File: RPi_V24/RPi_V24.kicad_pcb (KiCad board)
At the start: 4 copper layers, 65 x 56 mm, 61 parts, among them J1 DB9_Male, J10 Conn_01x03, J11 Conn_01x03, J12 Conn_01x03_Female, J13 Conn_02x04_Odd_Even, J14 Conn_01x03, J15 Conn_01x03, J16 Conn_02x05_Odd_Even, J17 Conn_02x05_Odd_Even, J18 Conn_02x05_Odd_Even, J2 DB9_Male, J3 40HAT, J4 DB9_Male, J5 Conn_02x04_Odd_Even, J6 Conn_01x03, J7 Conn_01x03, J8 Conn_02x04_Odd_Even, J9 CONN_01X02, U1 MAX561, U2 CAT24C32, U3 MAX561

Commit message: Now includes EN and SHDN for the transceivers.
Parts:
- added R16: 10K, Resistor_SMD:R_0402_1005Metric, F.Cu at (108.1, 91.6)
- added R17: 0R, Resistor_SMD:R_0402_1005Metric, F.Cu at (108.1, 89.7)
- added R18: 10K, Resistor_SMD:R_0402_1005Metric, F.Cu at (102.1, 72.3)
- added R19: 0R, Resistor_SMD:R_0402_1005Metric, F.Cu at (98.3, 73.9)
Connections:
- J13 pad 1: Net-(J13-Pad1) -> TXD4E
- J13 pad 7: Net-(J13-Pad7) -> RXD4E
- J3 pad 13: Net-(J3-Pad13) -> ~EN4_5
- J3 pad 15: Net-(J3-Pad15) -> SHDN4_5
- J3 pad 3: Net-(J3-Pad3) -> SHDN1_3
- J3 pad 5: Net-(J3-Pad5) -> ~EN1_3
- J5 pad 1: Net-(J5-Pad1) -> TXD1E
- J5 pad 7: Net-(J5-Pad7) -> RXD1E
- J8 pad 1: Net-(J8-Pad1) -> TXD3E
- J8 pad 7: Net-(J8-Pad7) -> RXD3E
- U1 pad 24: Net-(U1-Pad24) -> ~EN1_3
- U1 pad 25: Net-(U1-Pad25) -> SHDN1_3
- U3 pad 24: Net-(U3-Pad24) -> ~EN4_5
- U3 pad 25: Net-(U3-Pad25) -> SHDN4_5
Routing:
- net SHDN1_3: track 0.00 -> 50.4 mm, vias 0 -> 3
- net ~EN1_3: track 0.00 -> 46.5 mm, vias 0 -> 3
- net ~EN4_5: track 0.00 -> 16.6 mm, vias 0 -> 1
- net SHDN4_5: track 0.00 -> 10.1 mm, vias 0 -> 1
- net RXD3E: track 13.0 -> 15.8 mm
- net TX4DE: track 2.54 -> 0.00 mm
- net TX1DE: track 2.54 -> 0.00 mm
- net RXD4E: track 13.2 -> 15.7 mm
- net RX4DE: track 2.54 -> 0.00 mm
- net RX3DE: track 2.54 -> 0.00 mm
- net TXD1E: track 9.31 -> 11.9 mm
- net TXD3E: track 20.1 -> 22.7 mm
- net TX3DE: track 2.54 -> 0.00 mm
- net RXD1E: track 17.8 -> 20.3 mm
- net RX1DE: track 2.54 -> 0.00 mm
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
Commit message: Adds layer identifiers
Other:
- board text added: "1"
- board text added: "2"
- board text added: "3"
- board text added: "4"
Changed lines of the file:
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@@
   (general
     (thickness 1.6)
-    (drawings 131)
+    (drawings 135)
     (tracks 735)
     (zones 0)
@@
   (layers
     (0 F.Cu signal)
-    (1 In1.Cu power hide)
-    (2 In2.Cu power hide)
+    (1 In1.Cu power)
+    (2 In2.Cu power)
     (31 B.Cu signal)
     (32 B.Adhes user)
@@
       (drillshape 0)
       (scaleselection 1)
-      (outputdirectory "prod"))
+      (outputdirectory "../gerber/"))
   )
   (net 0 "")
@@
     )
   )
+  (gr_text 4 (at 126.238 115.316) (layer B.Cu)
+    (effects (font (size 1.5 1.5) (thickness 0.3)) (justify mirror))
+  )
+  (gr_text 3 (at 124.587 115.316) (layer In2.Cu)
+    (effects (font (size 1.5 1.5) (thickness 0.3)))
+  )
+  (gr_text 2 (at 122.809 115.316) (layer In1.Cu)
+    (effects (font (size 1.5 1.5) (thickness 0.3)))
+  )
+  (gr_text 1 (at 121.031 115.316) (layer F.Cu)
+    (effects (font (size 1.5 1.5) (thickness 0.3)))
+  )
   (gr_text + (at 89.408 106.68) (layer F.SilkS)
     (effects (font (size 0.6 0.6) (thickness 0.09)))
@@
       )
     )
+  )
+  (zone (net 0) (net_name "") (layers In1.Cu In2.Cu) (hatch edge 0.508)
+    (connect_pads (clearance 0.4))
+    (min_thickness 0.254)
+    (keepout (tracks allowed) (vias allowed) (copperpour not_allowed))
+    (fill (arc_segments 32) (thermal_gap 0.508) (thermal_bridge_width 0.508))
+    (polygon
+      (pts
+        (xy 127.254 117.221) (xy 120.015 117.221) (xy 120.015 113.665) (xy 127.254 113.665)
+      )
+    )

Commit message: Some final touches and some generated files.
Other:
- rule pad_to_mask_clearance: 0.1 -> 0.15
- board text added: "JLCJLCJLCJLC"
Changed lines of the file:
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@@
   (general
     (thickness 1.6)
-    (drawings 135)
+    (drawings 136)
     (tracks 735)
     (zones 0)
@@
     (pad_size 1.524 1.524)
     (pad_drill 0.762)
-    (pad_to_mask_clearance 0.1)
+    (pad_to_mask_clearance 0.15)
+    (solder_mask_min_width 0.153)
     (aux_axis_origin 0 0)
     (visible_elements 7FFFFE3F)
     (pcbplotparams
-      (layerselection 0x010f8_80000007)
+      (layerselection 0x010f8_ffffffff)
       (usegerberextensions false)
       (usegerberattributes false)
@@
     )
   )
+  (gr_text JLCJLCJLCJLC (at 104.521 76.708) (layer F.SilkS)
+    (effects (font (size 0.8 0.8) (thickness 0.15)))
+  )
   (gr_text 4 (at 126.238 115.316) (layer B.Cu)
     (effects (font (size 1.5 1.5) (thickness 0.3)) (justify mirror))
@@
   (segment (start 87.63 86.9525) (end 86.986999 87.595501) (width 0.25) (layer F.Cu) (net 66))
   (segment (start 93.853 79.121) (end 93.853 80.221) (width 0.25) (layer F.Cu) (net 66))
-  (segment (start 125.984 83.439) (end 125.984 85.979) (width 0.25) (layer F.Cu) (net 105))
-  (segment (start 125.984 89.721081) (end 125.984 91.059) (width 0.25) (layer F.Cu) (net 106))
-  (segment (start 125.984 88.519) (end 125.984 89.721081) (width 0.25) (layer F.Cu) (net 106))
-  (segment (start 107.442 99.314) (end 109.982 99.314) (width 0.25) (layer F.Cu) (net 108))
-  (segment (start 112.522 99.314) (end 115.062 99.314) (width 0.25) (layer F.Cu) (net 107))
-  (segment (start 96.393 89.594081) (end 96.393 90.932) (width 0.25) (layer F.Cu) (net 112))
-  (segment (start 96.393 88.392) (end 96.393 89.594081) (width 0.25) (layer F.Cu) (net 112))
-  (segment (start 96.393 83.312) (end 96.393 85.852) (width 0.25) (layer F.Cu) (net 111))
   (segment (start 134.8565 105.872) (end 135.001 105.7275) (width 0.15) (layer F.Cu) (net 75))
   (segment (start 133.35 105.872) (end 134.8565 105.872) (width 0.15) (layer F.Cu) (net 75))
@@
   (segment (start 89.027 86.36) (end 86.868 84.201) (width 0.25) (layer B.Cu) (net 104))
   (segment (start 89.027 87.0105) (end 89.027 86.36) (width 0.25) (layer B.Cu) (net 104))
+  (segment (start 125.984 83.439) (end 125.984 85.979) (width 0.25) (layer F.Cu) (net 105))
   (segment (start 126.1704 86.42901) (end 126.302205 86.297205) (width 0.25) (layer F.Cu) (net 105))
   (segment (start 122.428 83.693) (end 125.16401 86.42901) (width 0.25) (layer F.Cu) (net 105))
@@
   (segment (start 125.16401 86.42901) (end 126.1704 86.42901) (width 0.25) (layer F.Cu) (net 105))
   (segment (start 119.0675 84.914) (end 119.0675 84.26091) (width 0.25) (layer F.Cu) (net 105))
+  (segment (start 125.984 89.721081) (end 125.984 91.059) (width 0.25) (layer F.Cu) (net 106))
+  (segment (start 125.984 88.519) (end 125.984 89.721081) (width 0.25) (layer F.Cu) (net 106))
   (segment (start 123.317 82.705842) (end 123.317 82.423) (width 0.25) (layer B.Cu) (net 106))
   (segment (start 123.317 85.852) (end 123.317 82.705842) (width 0.25) (layer B.Cu) (net 106))
@@
   (segment (start 115.697 82.423) (end 123.034158 82.423) (width 0.25) (layer F.Cu) (net 106))
   (segment (start 123.034158 82.423) (end 123.317 82.423) (width 0.25) (layer F.Cu) (net 106))
+  (segment (start 112.522 99.314) (end 115.062 99.314) (width 0.25) (layer F.Cu) (net 107))
   (via (at 121.666 84.963) (size 0.4) (drill 0.2) (layers F.Cu B.Cu) (net 107))
   (segment (start 121.617 84.914) (end 121.666 84.963) (width 0.25) (layer F.Cu) (net 107))
@@
   (segment (start 112.522 99.314) (end 121.666 90.17) (width 0.25) (layer B.Cu) (net 107))
   (segment (start 121.666 85.245842) (end 121.666 84.963) (width 0.25) (layer B.Cu) (net 107))
+  (segment (start 107.442 99.314) (end 109.982 99.314) (width 0.25) (layer F.Cu) (net 108))
   (segment (start 119.0675 90.114) (end 119.0675 91.386504) (width 0.25) (layer F.Cu) (net 108))
   (segment (start 119.0675 91.386504) (end 118.616002 91.838002) (width 0.25) (layer F.Cu) (net 108))
@@
   (segment (start 101.0035 72.8095) (end 98.6155 70.4215) (width 0.25) (layer F.Cu) (net 110))
   (segment (start 101.0035 74.5315) (end 101.0035 72.8095) (width 0.25) (layer F.Cu) (net 110))
+  (segment (start 96.393 83.312) (end 96.393 85.852) (width 0.25) (layer F.Cu) (net 111))
   (via (at 98.933 85.598) (size 0.4) (drill 0.2) (layers F.Cu B.Cu) (net 111))
   (segment (start 98.679 85.852) (end 96.393 85.852) (width 0.25) (layer B.Cu) (net 111))
@@
   (segment (start 105.4485 80.5815) (end 104.369 81.661) (width 0.25) (layer F.Cu) (net 111))
   (segment (start 105.4485 79.7315) (end 105.4485 80.5815) (width 0.25) (layer F.Cu) (net 111))
+  (segment (start 96.393 89.594081) (end 96.393 90.932) (width 0.25) (layer F.Cu) (net 112))
+  (segment (start 96.393 88.392) (end 96.393 89.594081) (width 0.25) (layer F.Cu) (net 112))
   (segment (start 98.298 85.85059) (end 96.074795 88.073795) (width 0.25) (layer F.Cu) (net 112))
   (segment (start 98.298 83.187002) (end 98.298 85.85059) (width 0.25) (layer F.Cu) (net 112))

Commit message: Silk screen adjustments.
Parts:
- R17, R19: value 0R -> 10K

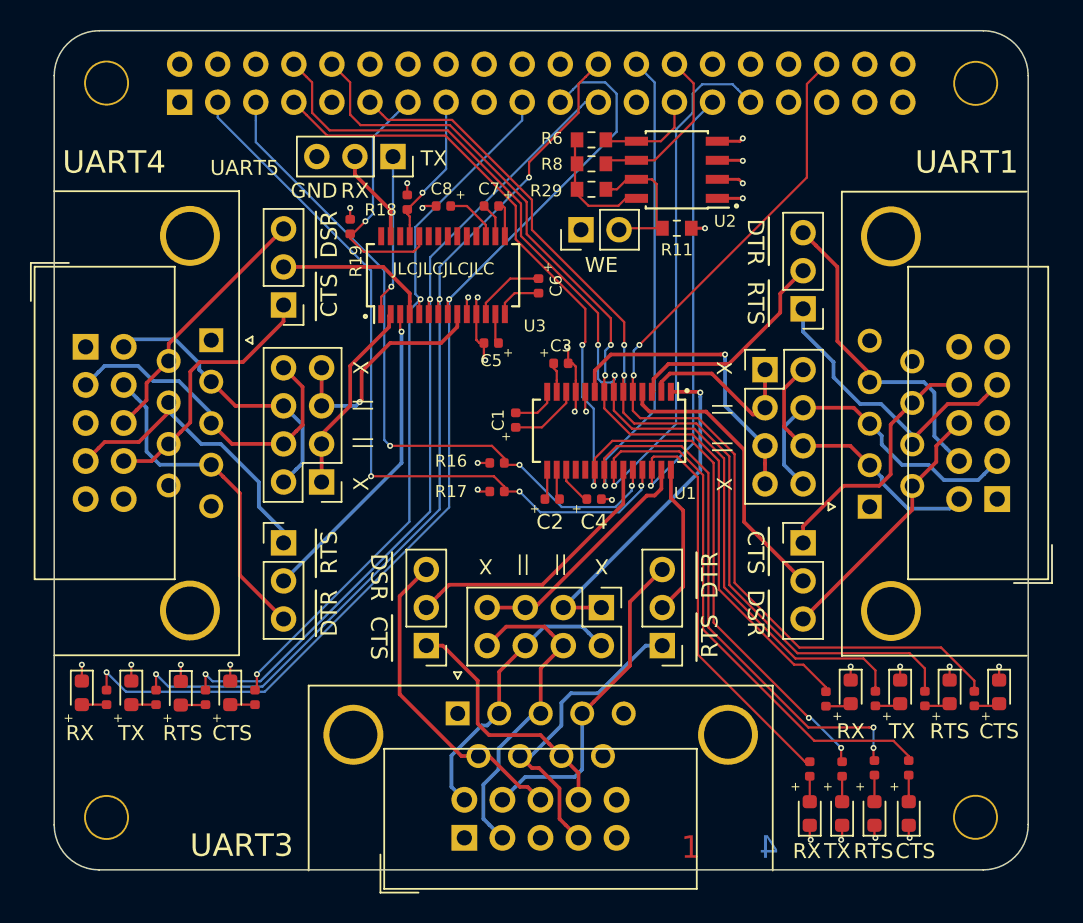
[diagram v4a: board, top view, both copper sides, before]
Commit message: Adjusts some component and trace positions
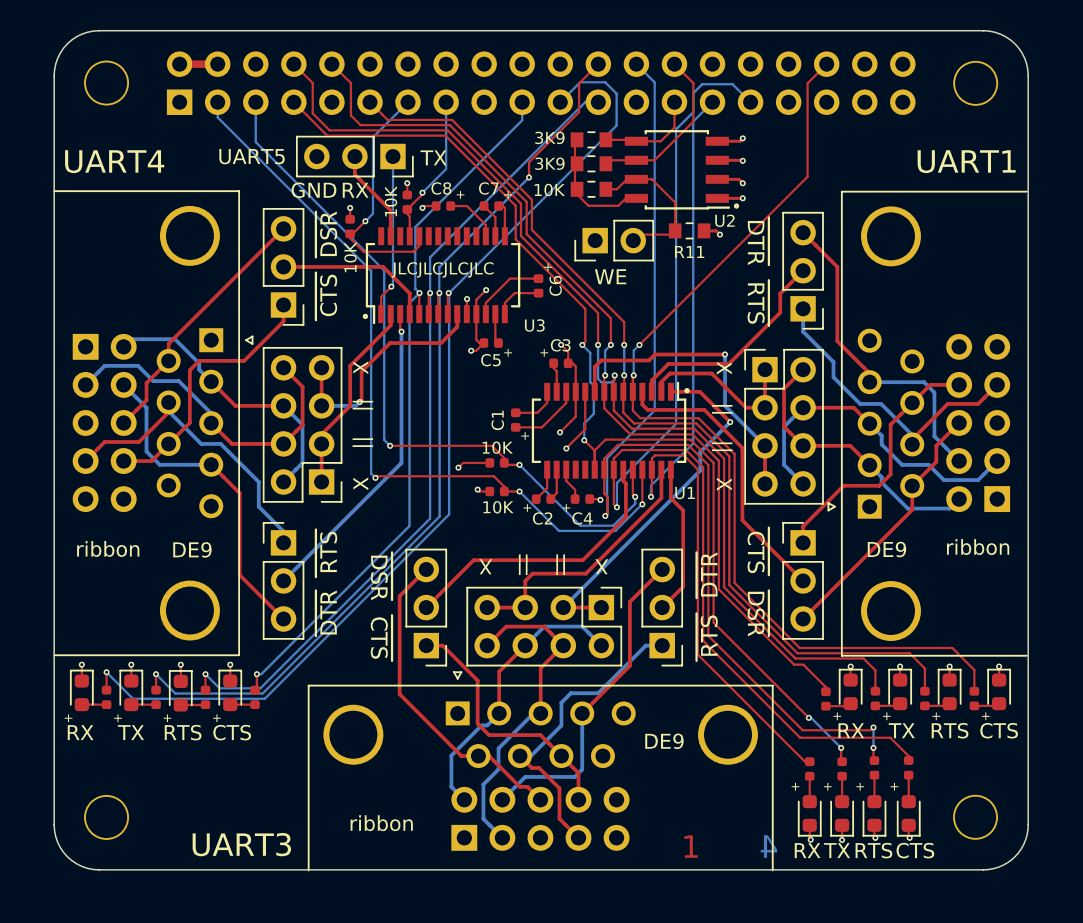
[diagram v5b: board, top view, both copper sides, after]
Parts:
- added G***: LOGO, LOGO, B.Cu at (111.5, 87.6)
- moved J9 1.20 mm to (114.7, 74.8)
- moved R11 0.87 mm to (121.0, 74.2)
- moved C4 0.78 mm to (113.8, 92.1)
- moved C2 0.58 mm to (111.2, 92.1)
- renumbered R29 to 10K, R16 to 10K, R17 to 10K, R18 to 10K, R19 to 10K, R8 to 3K9, R6 to 3K9
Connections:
- net ~EN1_3 renamed ~{EN1_3}
- net ~EN4_5 renamed ~{EN4_5}
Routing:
- net RTS3: track 66.2 -> 71.3 mm
- net GND: track 25.2 -> 29.8 mm
- net CTS3: track 69.4 -> 73.1 mm
- net P3V3_HAT: track 11.1 -> 13.8 mm
- net /P5V_HAT: track 0.00 -> 2.54 mm
- net RXD3: track 55.1 -> 57.0 mm
- net ~{EN1_3}: track 46.5 -> 48.3 mm
- net RXD3E: track 15.8 -> 17.6 mm
- net TXD3E: track 22.7 -> 24.3 mm
- net SHDN1_3: track 50.4 -> 52.0 mm
- net TXD3: track 73.1 -> 71.9 mm
- net RXD4: track 67.6 -> 68.7 mm
- net TXD4: track 60.4 -> 61.4 mm
- net RTS4: track 54.4 -> 55.5 mm
- net Net-(J9-Pad2): track 9.58 -> 10.5 mm
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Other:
- net class Default removed
- board text added: "DE9"
- board text added: "ribbon"
